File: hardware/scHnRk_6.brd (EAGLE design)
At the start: 99.9 x 47.6 mm, 48 parts, among them IC1 ATTINY87/167AUTOMOTIVETSSOP, J1 JUMPER, J2 JUMPER, J3 JUMPER, J4 JUMPER, J5 JUMPER, J6 JUMPER, SW1 SSAJ120100, SW2 L_BUTTON, SW3 R_BUTTON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

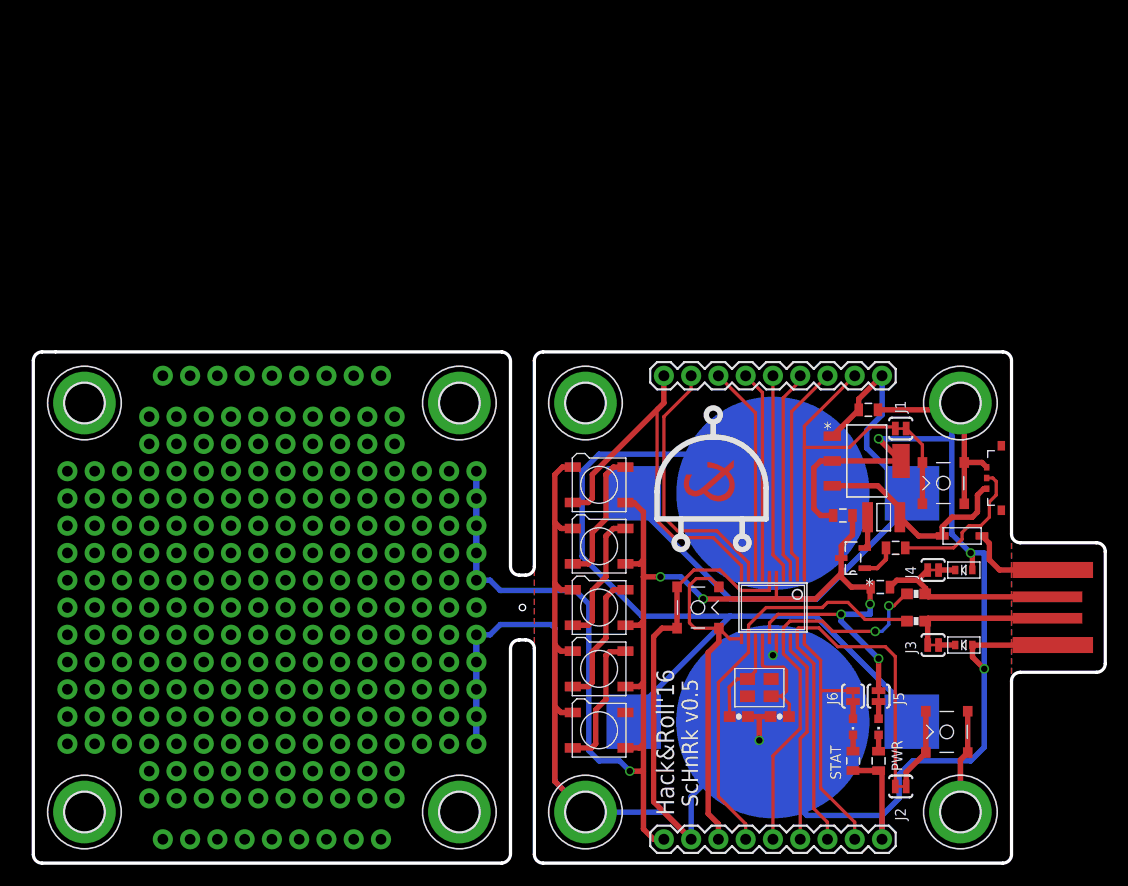
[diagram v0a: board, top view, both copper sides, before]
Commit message: added skeletons, transiting to atmega328p-mu
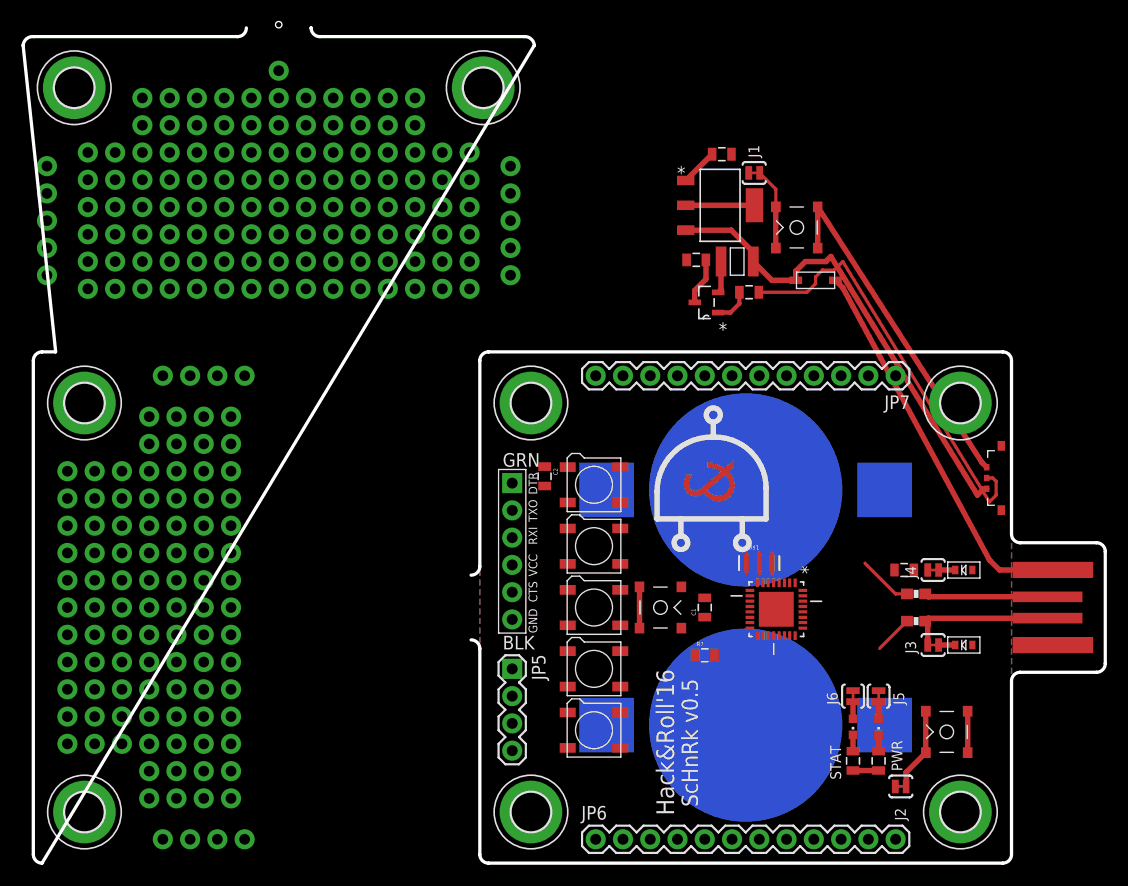
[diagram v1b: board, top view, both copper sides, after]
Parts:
- removed IC1: ATTINY87/167AUTOMOTIVETSSOP, attiny87_167_automotive:TSSOP20
- removed JP1, JP2: (no value), SparkFun-Connectors:1X09
- removed XTAL1: 16MHZ-2467444, scHnRk:16MHZ-2467444
- added JP4: FTDI_DEVICE, SparkFun-Connectors:FTDI_DEVICE_SIDE
- added JP5: (no value), SparkFun-Connectors:1X04
- added JP6, JP7: (no value), SparkFun-Connectors:1X12
- added R7: 10k, SparkFun-Passives:0805
- added U$1: 16MHZ, SparkFun-FreqCtrl:RESONATOR-SMD
- added U4: ATMEGA328P-MU, Atmel_By_element14_Batch_1-00:QFN50P500X500X100-33N
- C1, C2: value 9pF -> 0.1uF; device SparkFun-Passives:0603-CAP -> SparkFun-Passives:0805
- moved H1 67.5 mm to (41.9, 72.2), turned to 90 degrees
- moved H3 46.4 mm to (3.81, 72.2), turned to 90 degrees
- moved C2 28.8 mm to (47.6, 36.0), turned to 270 degrees
- moved C4 27.4 mm to (61.8, 56.2)
- moved D1 27.4 mm to (72.9, 54.3)
- moved F1 27.4 mm to (65.6, 56.0)
- moved R6 27.4 mm to (66.7, 53.2)
- moved U1 27.4 mm to (64.0, 61.3)
- moved U2 27.4 mm to (62.7, 52.2)
- moved C3 27.4 mm to (64.1, 66.0)
- moved J1 27.4 mm to (67.2, 64.3)
- moved SW2 27.4 mm to (71.1, 59.2)
- moved C1 12.3 mm to (62.5, 23.8), turned to 90 degrees
- moved H5 5.08 mm to (46.4, 4.76)
- moved H7 5.08 mm to (46.4, 42.9)
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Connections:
- removed net D0/SCA/LED: IC1.20, J6.2, JP2.8
- removed net D1/LB: IC1.19, J2.1, JP2.7
- removed net D10/A10/MOSI: IC1.7, JP1.4
- removed net D11/A11/SCK: IC1.8, JP1.3
- removed net D12/A12/SS: IC1.9, JP1.2
- removed net D13/A13: IC1.10, JP1.1, LED1.4-DIN
- removed net D2/SCL: IC1.18, JP2.6
- removed net D4/A4: IC1.12, JP2.4, R3.2
- removed net D6/A6/RB: IC1.1, J1.1, JP1.8
- removed net D7/A7: IC1.2, JP1.7
- removed net D8/A8/MISO: IC1.3, JP1.6
- removed net D9/A9: IC1.4, JP1.5
- new net A0: U4.23
- new net A1: U4.24
- new net A2: U4.25
- new net A3: U4.26
- new net A4/SDA: JP5.3, U4.27
- new net A5/SCL: JP5.4, U4.28
- new net A6: U4.19
- new net A7: U4.22
- new net D0/RXD: JP4.P$2, JP7.1, U4.30
- new net D1/TXD: JP4.P$3, JP7.2, U4.31
- new net D10: U4.14
- new net D11/MOSI: U4.15
- new net D12/MISO: U4.16
- new net D13/SCK: J6.2, U4.17
- new net D2: R3.2, U4.32
- new net D4: JP7.4, U4.2
- new net D5: JP7.5, U4.9
- new net D6: JP7.6, U4.10
- new net D7: R2.2, U4.11
- new net D8: JP7.7, U4.12
- new net D9: U4.13
- new net HEATSINK: U4.33
- new net N$21: JP7.12
- new net N$23: JP7.11
- new net N$25: C2.2, JP4.P$1
- new net N$256: JP6.12
- new net N$26: LED1.4-DIN
- new net N$264: JP6.11
- new net N$265: JP6.10
- new net N$266: JP6.9
- new net N$267: JP6.8
- new net N$268: JP6.7
- new net N$269: JP6.6
- new net N$271: JP6.5
- new net N$272: JP6.4
- new net N$273: JP6.3
- new net N$274: JP6.2
- new net N$285: JP6.1
- new net N$307: J1.1
- new net N$308: J2.1
- new net N$62: C1.2, U4.20
- new net N$81: JP7.10
- new net N$84: JP7.9
- new net N$85: JP7.8
- net 5V: now also JP4.P$4, JP5.2, R7.1, U4.18, U4.4, U4.6; no longer IC1.15, IC1.5, JP2.1
- net D3: now also JP7.3, U4.1; no longer IC1.17, JP2.5, R2.2
- net GND: now also C1.1, JP4.P$5, JP4.P$6, JP5.1, U$1.2, U4.21, U4.3, U4.5; no longer C1.2, C2.2, H5.B3,6, H6.B3,6, H8.B3,6, IC1.16, IC1.6, JP2.2, JP2.9
- net RESET: now also C2.1, R7.2, U4.29; no longer IC1.11, JP2.3
- net VBATT: no longer JP1.9
- net XTAL1: now also U$1.3, U4.7; no longer C1.1, IC1.14, XTAL1.P$1
- net XTAL2: now also U$1.1, U4.8; no longer C2.1, IC1.13, XTAL1.P$3
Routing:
- net GND: track 305.0 -> 49.3 mm, vias 10 -> 0
- net 5V: track 136.3 -> 4.40 mm, vias 11 -> 0
- net N$1: track 79.5 -> 0.00 mm
- net VBATT: track 57.1 -> 3.47 mm
- net D1/LB: track 43.1 -> 0.00 mm
- net D4/A4: track 38.5 -> 0.00 mm
- net D13/A13: track 37.2 -> 0.00 mm
- net D3: track 36.5 -> 0.00 mm, vias 2 -> 0
- net RESET: track 32.8 -> 0.00 mm
- net D6/A6/RB: track 29.9 -> 0.00 mm
- net USBVCC: track 8.81 -> 36.1 mm
- net D12/A12/SS: track 25.1 -> 0.00 mm
- net N$7: track 14.0 -> 38.8 mm
- net PRE5V: track 20.1 -> 44.6 mm
- net D0/SCA/LED: track 23.6 -> 0.00 mm
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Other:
- board size 99.9 x 47.6 mm -> 100.8 x 77.8 mm
